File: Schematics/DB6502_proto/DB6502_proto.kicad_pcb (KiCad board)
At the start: 2 copper layers, 102 parts, among them J1 Controls, J10 LCD Port, J11 VIA Ports, J12 Power plug, J2 AVR ISP, J3 Debug USB, J4 Debug UART, J5 UART A, J6 UART B, J7 I/O Bus, J8 System Bus, J9 Clock divider, SW1 Reset, U1 71256, U10 FT230XS, U11 74HC595, U12 74HC157, U13 ATmega644PA-PU, U14 74AC74, U15 DS1813, U16 74AC74, U17 74AC08, U18 SC26C92, U19 65C22S, U2 71256, U3 28C256, U4 65C02S, U5 74AC74, U6 74AC138, U7 22V10C, U8 74AC04, U9 74HC21, X1 8MHz, Y1 20MHz, Y2 3,6864MHz

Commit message: Most chips placed, tracing continues
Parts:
- removed C11: 10nF, Capacitor_THT:C_Disc_D5.0mm_W2.5mm_P2.50mm
- removed FB1: FB, Resistor_THT:R_Axial_DIN0207_L6.3mm_D2.5mm_P10.16mm_Horizontal
- added R20: 4K7, Resistor_THT:R_Axial_DIN0207_L6.3mm_D2.5mm_P10.16mm_Horizontal, F.Cu at (383.5, 101.6)
- added R21: 10K, Resistor_THT:R_Axial_DIN0207_L6.3mm_D2.5mm_P10.16mm_Horizontal, F.Cu at (378.5, 101.6)
- C21, C22: moved to F.Cu
- moved R5 387.1 mm to (405.1, 80.0), turned to 180 degrees
- moved R15 374.2 mm to (405.1, 86.4), turned to 180 degrees
- moved R16 346.5 mm to (405.1, 92.7), turned to 180 degrees
- moved C13 342.6 mm to (383.5, 63.5), turned to 90 degrees
- moved U10 340.3 mm to (381.0, 71.1)
- moved C22 333.4 mm to (383.5, 80.0)
- moved C21 333.0 mm to (383.5, 85.1)
- moved C12 331.0 mm to (378.5, 63.5), turned to 90 degrees
- moved R13 322.9 mm to (368.3, 80.0)
- moved D2 319.7 mm to (388.6, 86.4)
- moved R14 305.0 mm to (368.3, 85.1)
- moved D3 295.1 mm to (388.6, 92.7)
- moved R1 192.9 mm to (363.2, 139.7)
- moved C7 159.1 mm to (367.0, 144.8)
- moved TP2 155.6 mm to (374.6, 144.8)
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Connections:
- U10 pad 16: Net-(U10-Pad16) -> VBUS_SENSE
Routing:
- net +5V: track 106.2 -> 314.4 mm, vias 2 -> 3
- net ROM_~CS: track 0.00 -> 92.3 mm, vias 0 -> 1
- net a8: track 113.2 -> 204.7 mm, vias 3 -> 4
- net a12: track 145.4 -> 232.8 mm, vias 3 -> 4
- net a9: track 110.4 -> 196.6 mm, vias 2 -> 3
- net a14: track 138.9 -> 223.4 mm, vias 3 -> 4
- net a13: track 127.2 -> 207.3 mm, vias 4 -> 5
- net a11: track 120.6 -> 198.8 mm, vias 4 -> 5
- net a7: track 138.3 -> 215.2 mm, vias 3 -> 5
- net a10: track 108.5 -> 184.2 mm, vias 3 -> 4
- net a6: track 131.6 -> 204.1 mm, vias 3 -> 5
- net RAM2_~CS: track 0.00 -> 69.6 mm, vias 0 -> 1
- net a5: track 126.1 -> 194.3 mm, vias 3 -> 5
- net RAM1_~CS: track 0.00 -> 60.9 mm
- net a0: track 114.2 -> 171.4 mm, vias 2 -> 3
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
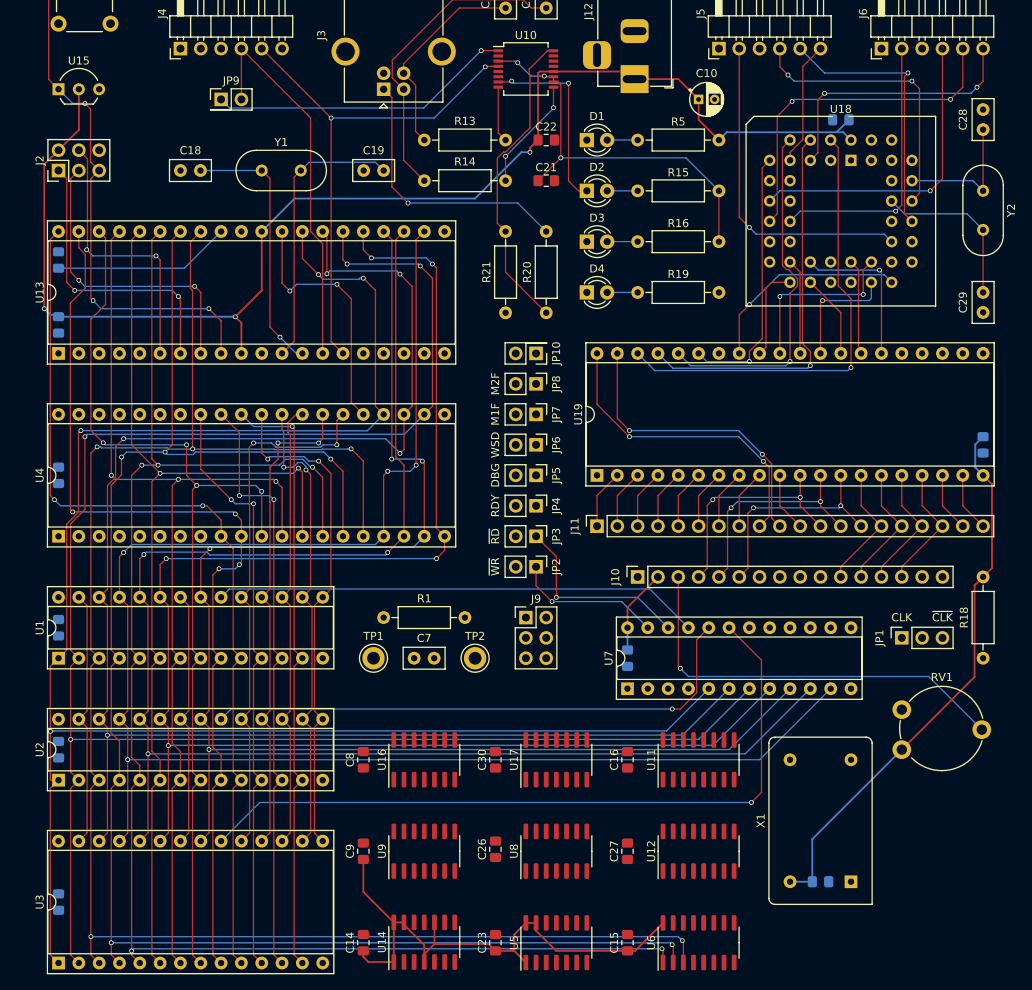
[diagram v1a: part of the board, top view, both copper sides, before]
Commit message: Most of the traces created
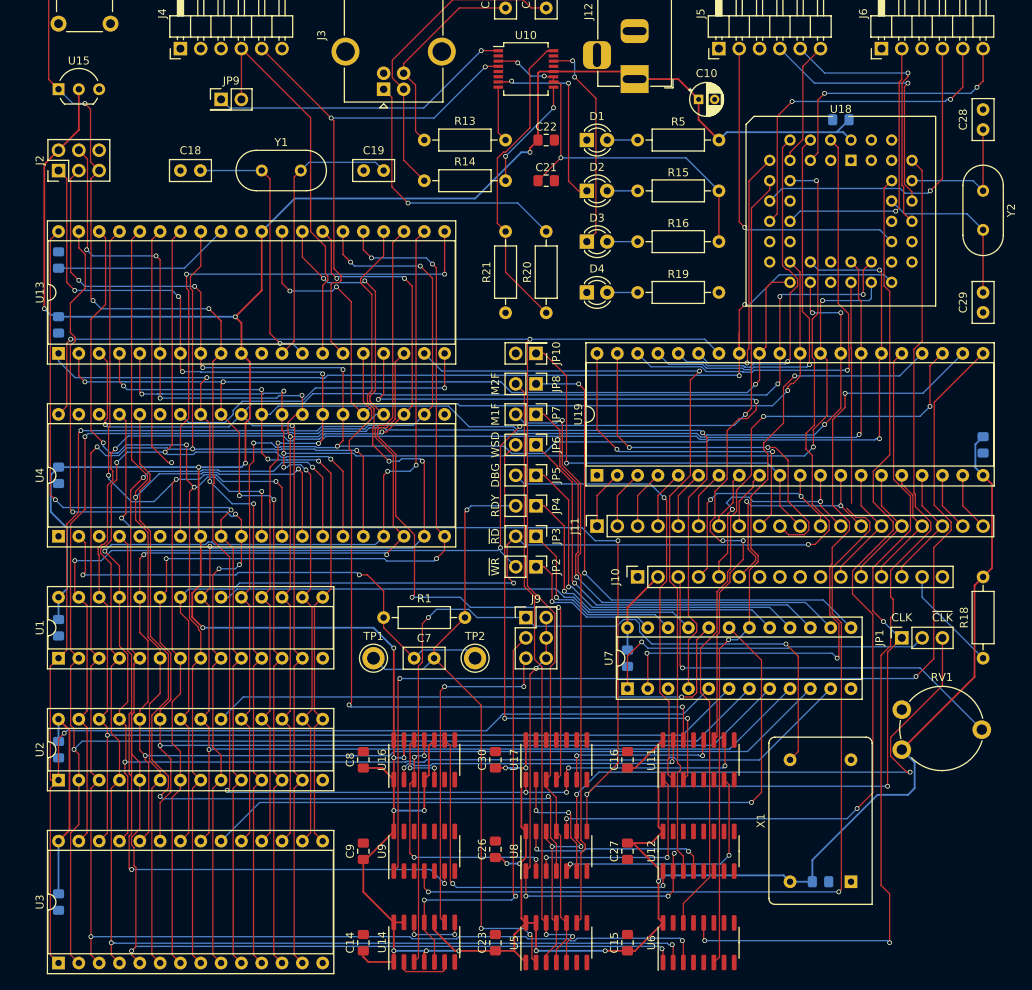
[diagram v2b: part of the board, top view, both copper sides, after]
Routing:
- net +5V: track 314.4 -> 583.9 mm, vias 3 -> 21
- net 6502_CLK: track 0.00 -> 212.4 mm, vias 0 -> 5
- net ~6502_RES: track 0.00 -> 173.3 mm, vias 0 -> 2
- net ~RD: track 32.2 -> 170.7 mm, vias 0 -> 3
- net ~WR: track 32.2 -> 169.5 mm, vias 0 -> 4
- net ~VIA1_IRQ: track 0.00 -> 134.6 mm, vias 0 -> 2
- net ~UART_IRQ: track 0.00 -> 134.2 mm, vias 0 -> 2
- net ~UART: track 0.00 -> 128.4 mm, vias 0 -> 2
- net ~RES: track 71.3 -> 197.7 mm, vias 3 -> 8
- net UART_RES: track 0.00 -> 123.5 mm, vias 0 -> 2
- net R~W: track 0.00 -> 121.4 mm, vias 0 -> 4
- net BE: track 0.00 -> 110.9 mm, vias 0 -> 2
- net Net-(J9-Pad1): track 0.00 -> 107.6 mm, vias 0 -> 2
- net d5: track 101.6 -> 207.6 mm, vias 2 -> 8
- net d4: track 74.2 -> 179.4 mm, vias 3 -> 7
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
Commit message: Moved things around, board starts to have shape
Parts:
- moved C13 287.9 mm to (96.5, 40.6)
- moved C19 287.9 mm to (73.7, 61.0)
- moved C21 287.9 mm to (96.5, 62.2)
- moved C22 287.9 mm to (96.5, 57.1)
- moved J10 287.9 mm to (108.0, 111.8)
- moved J3 287.9 mm to (76.2, 50.8)
- moved R1 287.9 mm to (76.2, 116.8)
- moved R19 287.9 mm to (108.0, 76.2)
- moved R20 287.9 mm to (96.5, 78.7)
- moved Y1 287.9 mm to (61.0, 61.0)
- moved C1 287.9 mm to (35.6, 80.3)
- moved C10 287.9 mm to (115.6, 52.1)
- moved C12 287.9 mm to (91.4, 40.6)
- moved C14 287.9 mm to (73.7, 157.5)
- moved C15 287.9 mm to (106.7, 157.5)
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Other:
- board outline added: 143.5 x 138.4 mm

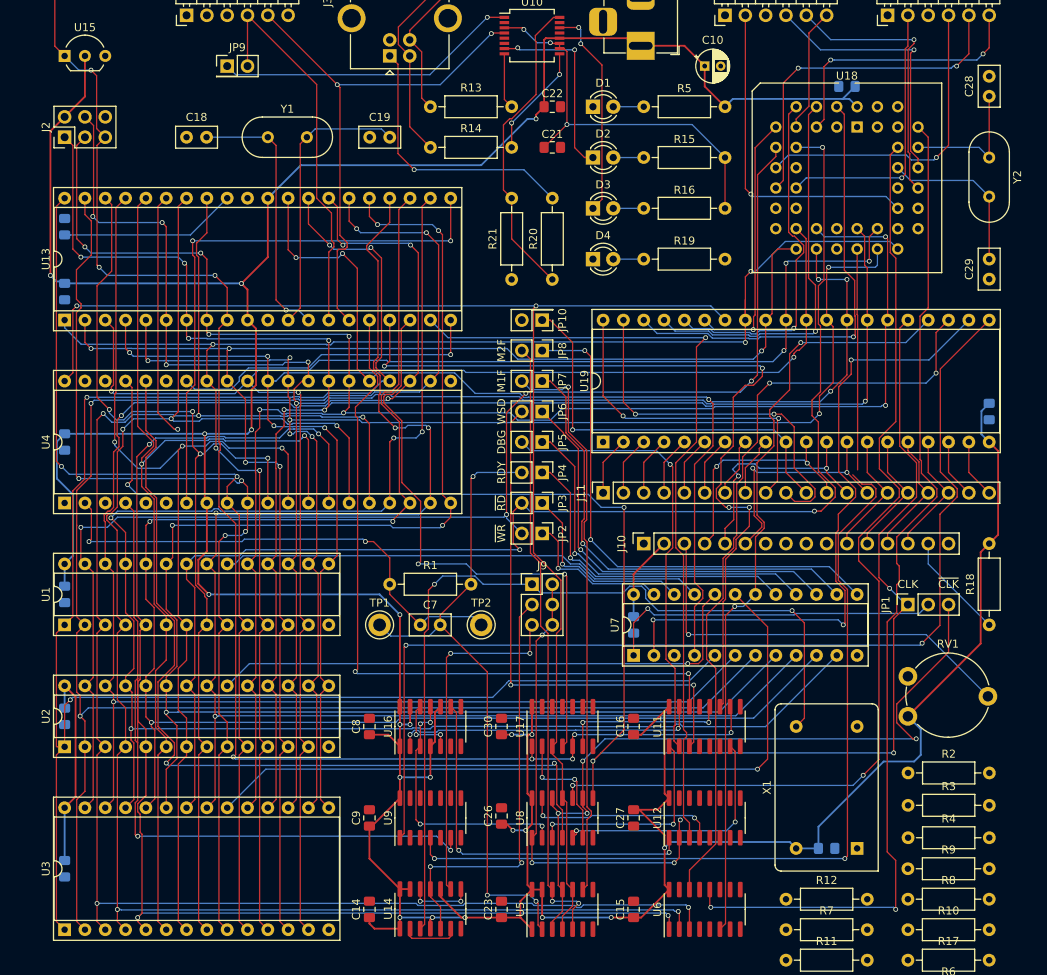
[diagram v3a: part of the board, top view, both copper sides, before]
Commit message: Increased capacitor footprints to 1206
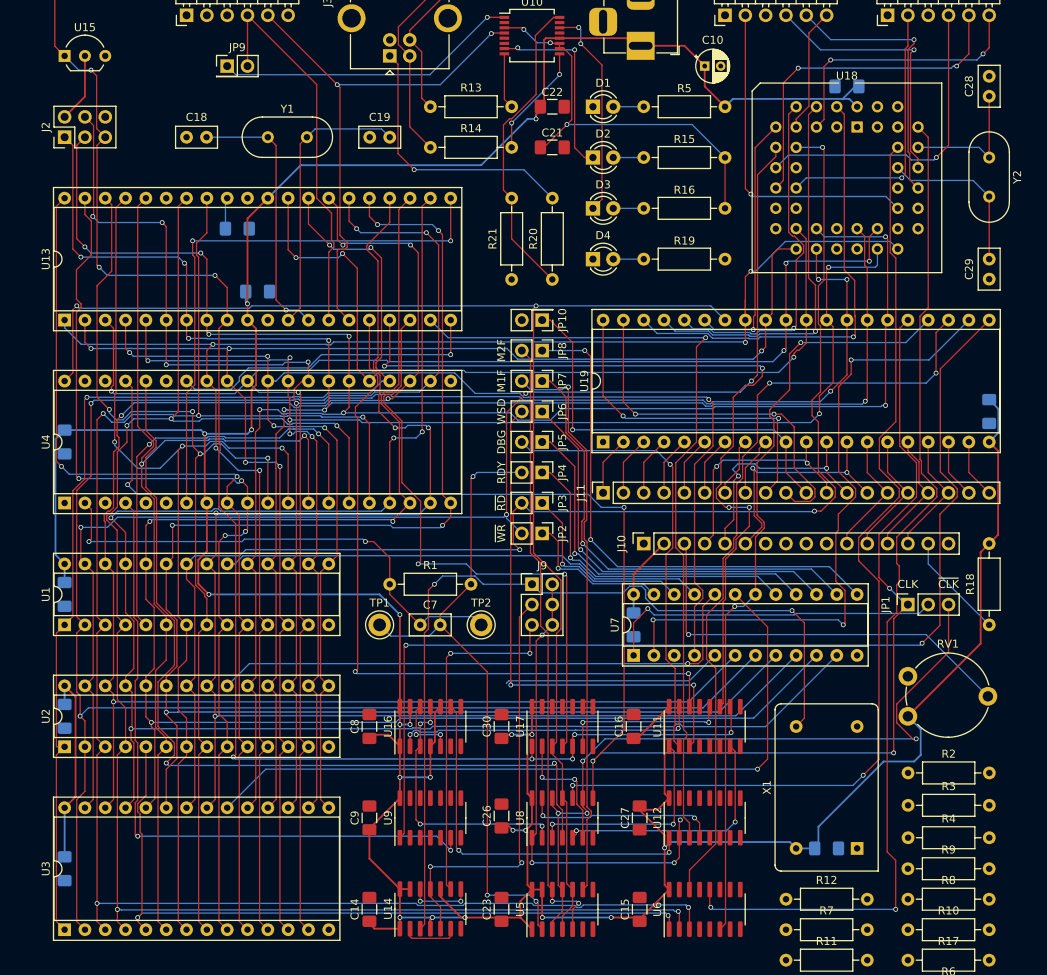
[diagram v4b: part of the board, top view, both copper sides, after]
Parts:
- C1, C14, C15, C16, C17, C2, C20, C21, C22, C23, C24, C25, C26, C27, C3, C30, C4, C5, C6, C8, C9: footprint Capacitor_SMD:C_0805_2012Metric_Pad1.15x1.40mm_HandSolder -> Capacitor_SMD:C_1206_3216Metric_Pad1.42x1.75mm_HandSolder
- moved C1 24.1 mm to (59.7, 80.3), turned to 0 degrees
- moved C20 21.6 mm to (57.1, 72.4), turned to 180 degrees
- moved C15 0.76 mm to (107.4, 157.5)
- moved C27 0.76 mm to (107.4, 146.1)
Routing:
- net ~UART_IRQ: track 134.2 -> 0.00 mm, vias 2 -> 0
- net a14: track 228.5 -> 167.0 mm, vias 4 -> 3
- net a5: track 194.5 -> 147.8 mm, vias 5 -> 4
- net +5V: track 583.9 -> 540.6 mm, vias 21 -> 20
- net Net-(C20-Pad2): track 22.2 -> 3.90 mm
- net ~IRQ: track 92.3 -> 84.3 mm

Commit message: Some cosmetic updates
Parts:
- moved C16 0.76 mm to (107.4, 134.6)
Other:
- board text added: "/1"
- board text added: "/2"
- board text added: "/4"
- board text added: "22V10 PLD"
- board text added: "65C02 CPU"
- board text added: "65C22 VIA"
- board text added: "ATMega644 Supervisor"
- board text added: "AVR ISP"
- board text added: "Blink"
- board text added: "Debug RXD Enable"
- board text added: "Debug UART Port"
- board text added: "Debug USB Port"
- board text added: "LCD Port"
- board text added: "PWR"
- board text added: "Power"
- board text added: "RAM 1"
- board text added: "RAM 2"
- board text added: "ROM"
- board text added: "RX"
- board text added: "SC26C92 UART"
- board text added: "TX"
- board text added: "UART Port A"
- board text added: "UART Port B"
- board text added: "VIA Port"

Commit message: Updates and fixes
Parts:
- removed R11, R6, R9: 4K7, Resistor_THT:R_Axial_DIN0207_L6.3mm_D2.5mm_P10.16mm_Horizontal
- J1, J7: footprint Connector_PinSocket_2.54mm:PinSocket_1x32_P2.54mm_Vertical -> Connector_PinSocket_2.54mm:PinSocket_1x40_P2.54mm_Vertical
- JP1: footprint Connector_PinSocket_2.54mm:PinSocket_1x03_P2.54mm_Vertical -> Connector_PinHeader_2.54mm:PinHeader_1x03_P2.54mm_Vertical
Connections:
- J1 pad 1: ~RES -> +5V
- J1 pad 10: ~6502_RES -> ~NMI
- J1 pad 11: 6502_CLK -> ~SO
- J1 pad 12: R~W -> ~6502_RES
- J1 pad 13: EXRAM -> 6502_CLK
- J1 pad 14: SR_DAT -> R~W
- J1 pad 15: SR_CLK -> EXRAM
- J1 pad 16: SR_OUT -> Net-(J1-Pad16)
- J1 pad 17: DBG_CLK -> Net-(J1-Pad17)
- J1 pad 18: RDY_M1F -> Net-(J1-Pad18)
- J1 pad 19: RDY_M2F -> DBG_CLK
- J1 pad 2: SYNC -> GND
- J1 pad 20: WS_DISABLE -> RDY_M1F
- J1 pad 21: DBG_WAIT -> RDY_M2F
- J1 pad 22: 6502_RDY -> WS_DISABLE
- J1 pad 23: d0 -> DBG_WAIT
- J1 pad 24: d1 -> 6502_RDY
- J1 pad 25: d2 -> d0
- J1 pad 26: d3 -> d1
- J1 pad 27: d4 -> d2
- J1 pad 28: d5 -> d3
- J1 pad 29: d6 -> d4
- J1 pad 3: ~ML -> ~RES
- J1 pad 30: d7 -> d5
- J1 pad 31: +5V -> d6
- J1 pad 32: GND -> d7
- J1 pad 4: ~VP -> SYNC
- J1 pad 5: 6502_RDY -> ~ML
- J1 pad 6: BE -> ~VP
- J1 pad 7: ~IRQ -> 6502_RDY
- J1 pad 8: ~NMI -> BE
- J1 pad 9: ~SO -> ~IRQ
- J7 pad 1: a0 -> +5V
- J7 pad 10: d4 -> d2
- J7 pad 11: d5 -> d3
- J7 pad 12: d6 -> d4
- J7 pad 13: d7 -> d5
- J7 pad 14: IOCS -> d6
- J7 pad 15: ~LATCH -> d7
- J7 pad 16: ~VIA1 -> IOCS
- J7 pad 17: ~VIA2 -> ~LATCH
- J7 pad 18: ~UART -> ~VIA1
- J7 pad 19: ~IOCS0 -> ~VIA2
- J7 pad 2: a1 -> GND
- J7 pad 20: ~IOCS1 -> ~UART
- J7 pad 21: ~IOCS2 -> ~IOCS0
- J7 pad 22: ~IOCS3 -> ~IOCS1
- J7 pad 23: ~RD -> ~IOCS2
- J7 pad 24: ~WR -> ~IOCS3
- J7 pad 25: ~6502_RES -> ~RD
- J7 pad 26: R~W -> ~WR
- J7 pad 27: CLK -> ~6502_RES
- J7 pad 28: RAM1_~CS -> R~W
- J7 pad 29: RAM2_~CS -> 6502_CLK
- J7 pad 3: a2 -> a0
- J7 pad 30: ROM_~CS -> RAM1_~CS
- J7 pad 31: +5V -> RAM2_~CS
- J7 pad 32: GND -> ROM_~CS
- J7 pad 4: a3 -> a1
- J7 pad 5: a4 -> a2
- J7 pad 6: d0 -> a3
- J7 pad 7: d1 -> a4
- J7 pad 8: d2 -> d0
- J7 pad 9: d3 -> d1
